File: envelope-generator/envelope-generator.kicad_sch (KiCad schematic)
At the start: 28 parts, among them J1 Power, J2 Power, J3 Pot, J4 Pot, J5 Gate Input, J7 Output, SW1 Gate Button, SW2 AR/D Switch, U1 TL072

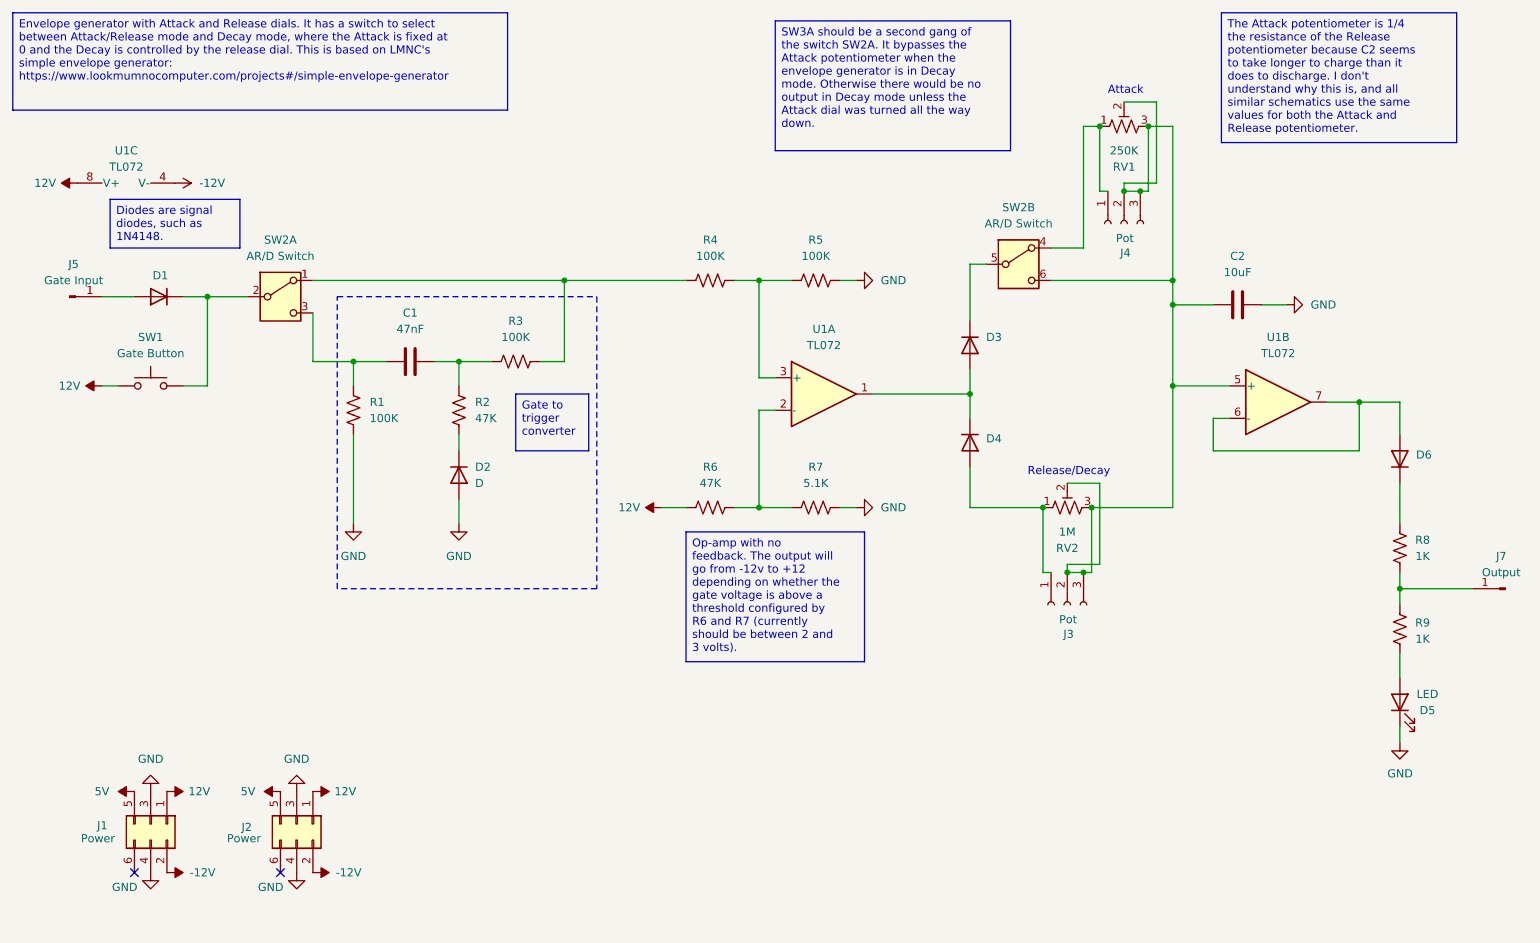
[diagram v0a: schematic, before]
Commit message: Envelope generator fixes
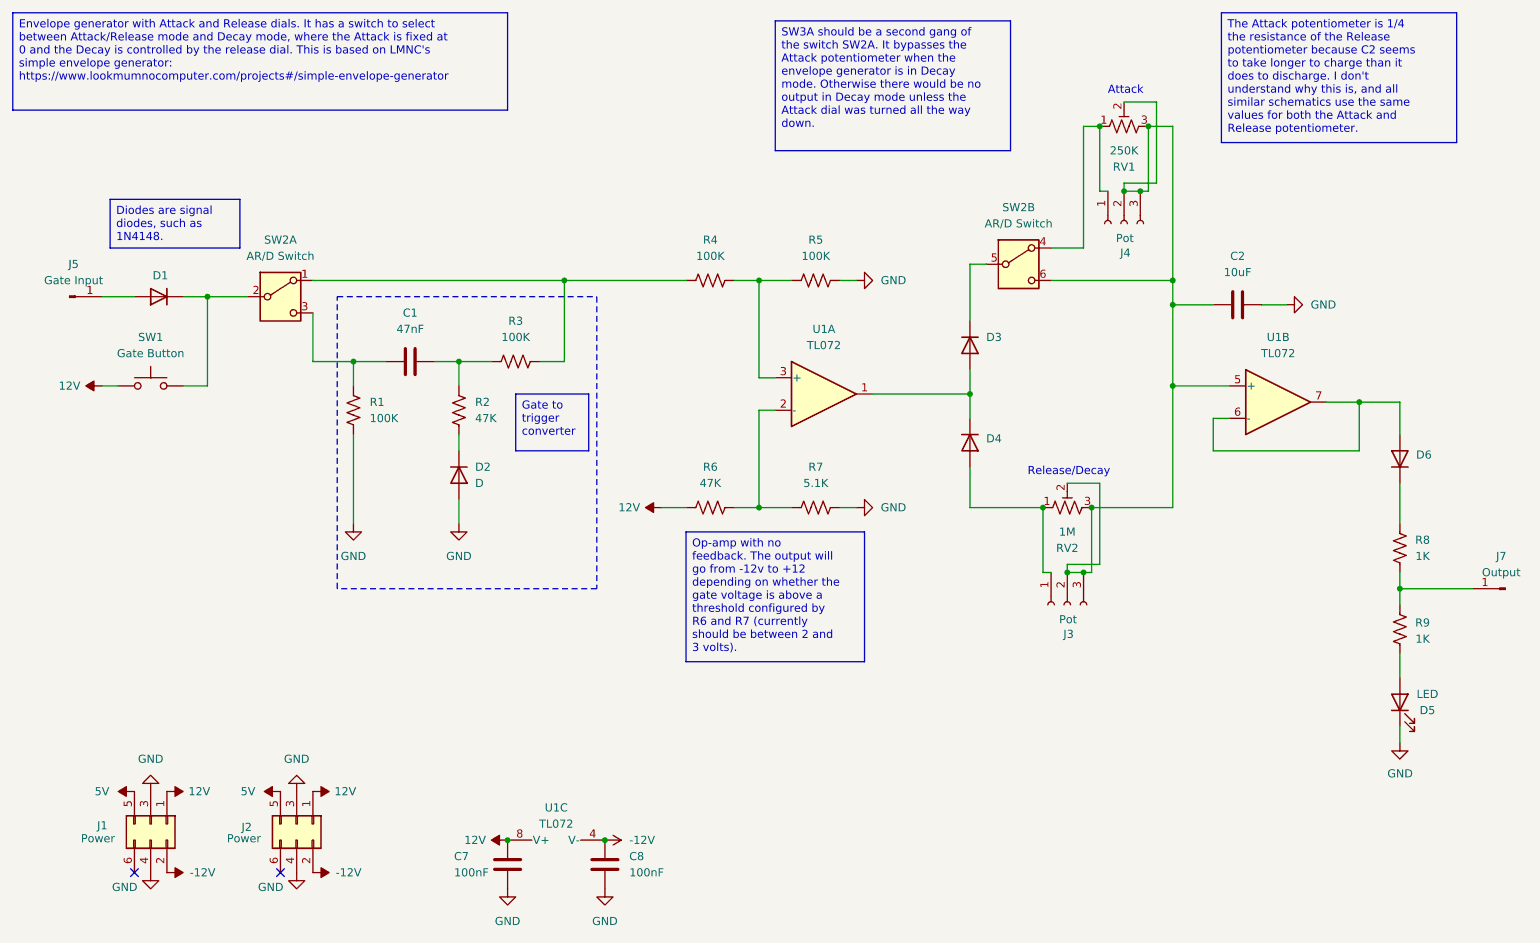
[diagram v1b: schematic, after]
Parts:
- added C7, C8: 100nF, Capacitor_THT:C_Disc_D4.3mm_W1.9mm_P5.00mm, symbol Device:C
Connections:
- net -12V: now also C8.2
- net 12V: now also C7.2
- net GND: now also C7.1, C8.1
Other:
- moved on the sheet: U1C

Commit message: Various improvements
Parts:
- SW1: footprint modular2:button1 -> Button_Switch_Keyboard:SW_Cherry_MX_1.00u_PCB
- renumbered C7 to C3, C8 to C4
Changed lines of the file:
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@@
 		(on_board yes)
 		(dnp no)
-		(property "Reference" "C7"
+		(property "Reference" "C3"
 			(at 104.648 151.13 0)
 			(effects
@@
 			(project "envelope-generator"
 				(path "/507f021b-704c-4b75-989e-31405ea53b96"
-					(reference "C7")
+					(reference "C3")
 					(unit 1)
 				)
@@
 			)
 		)
-		(property "Footprint" "modular2:button1"
+		(property "Footprint" "Button_Switch_Keyboard:SW_Cherry_MX_1.00u_PCB"
 			(at 57.15 72.39 0)
 			(effects
@@
 		(dnp no)
 		(fields_autoplaced yes)
-		(property "Reference" "C8"
+		(property "Reference" "C4"
 			(at 132.08 151.1299 0)
 			(effects
@@
 			(project "envelope-generator"
 				(path "/507f021b-704c-4b75-989e-31405ea53b96"
-					(reference "C8")
-					(unit 1)
-				)
+					(reference "C4")
+					(unit 1)
+				)
